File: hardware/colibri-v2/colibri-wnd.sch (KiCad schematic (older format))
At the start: 0 parts

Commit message: Work on GPS. Added PCA9685
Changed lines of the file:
@@
 $Descr A3 16535 11693
 encoding utf-8
-Sheet 1 25
+Sheet 1 26
 Title "Colibri WND"
 Date ""
@@
 	5350 4000 5750 4000
 Wire Wire Line
-	5750 4000 5750 6200
+	5750 4000 5750 5550
+Wire Wire Line
+	5750 5550 5750 6200
 Wire Wire Line
 	5750 6200 5350 6200
@@
 Text Notes 5500 2300 0    60   ~ 0
 Connect BUTTON_0 to:\nPB2/BOOT1
+$Sheet
+S 12850 8100 1850 750
+U 566CBCE8
+F0 "LED Controller" 60
+F1 "pca9685pw_led_ctrl.sch" 60
+F2 "PCA9685_OE(3V3)" I L 12850 8200 60
+F3 "PCA9865_I2C_SCL" I L 12850 8300 60
+F4 "PCA9865_I2C_SDA" B L 12850 8400 60
+$EndSheet
 $EndSCHEMATC

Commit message: Added connection between wandboard and cortex USB FS2
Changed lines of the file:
@@
 $Descr A3 16535 11693
 encoding utf-8
-Sheet 1 26
+Sheet 1 27
 Title "Colibri WND"
 Date ""
@@
 	5350 4000 5750 4000
 Wire Wire Line
-	5750 4000 5750 5550
-Wire Wire Line
-	5750 5550 5750 6200
+	5750 4000 5750 6200
 Wire Wire Line
 	5750 6200 5350 6200

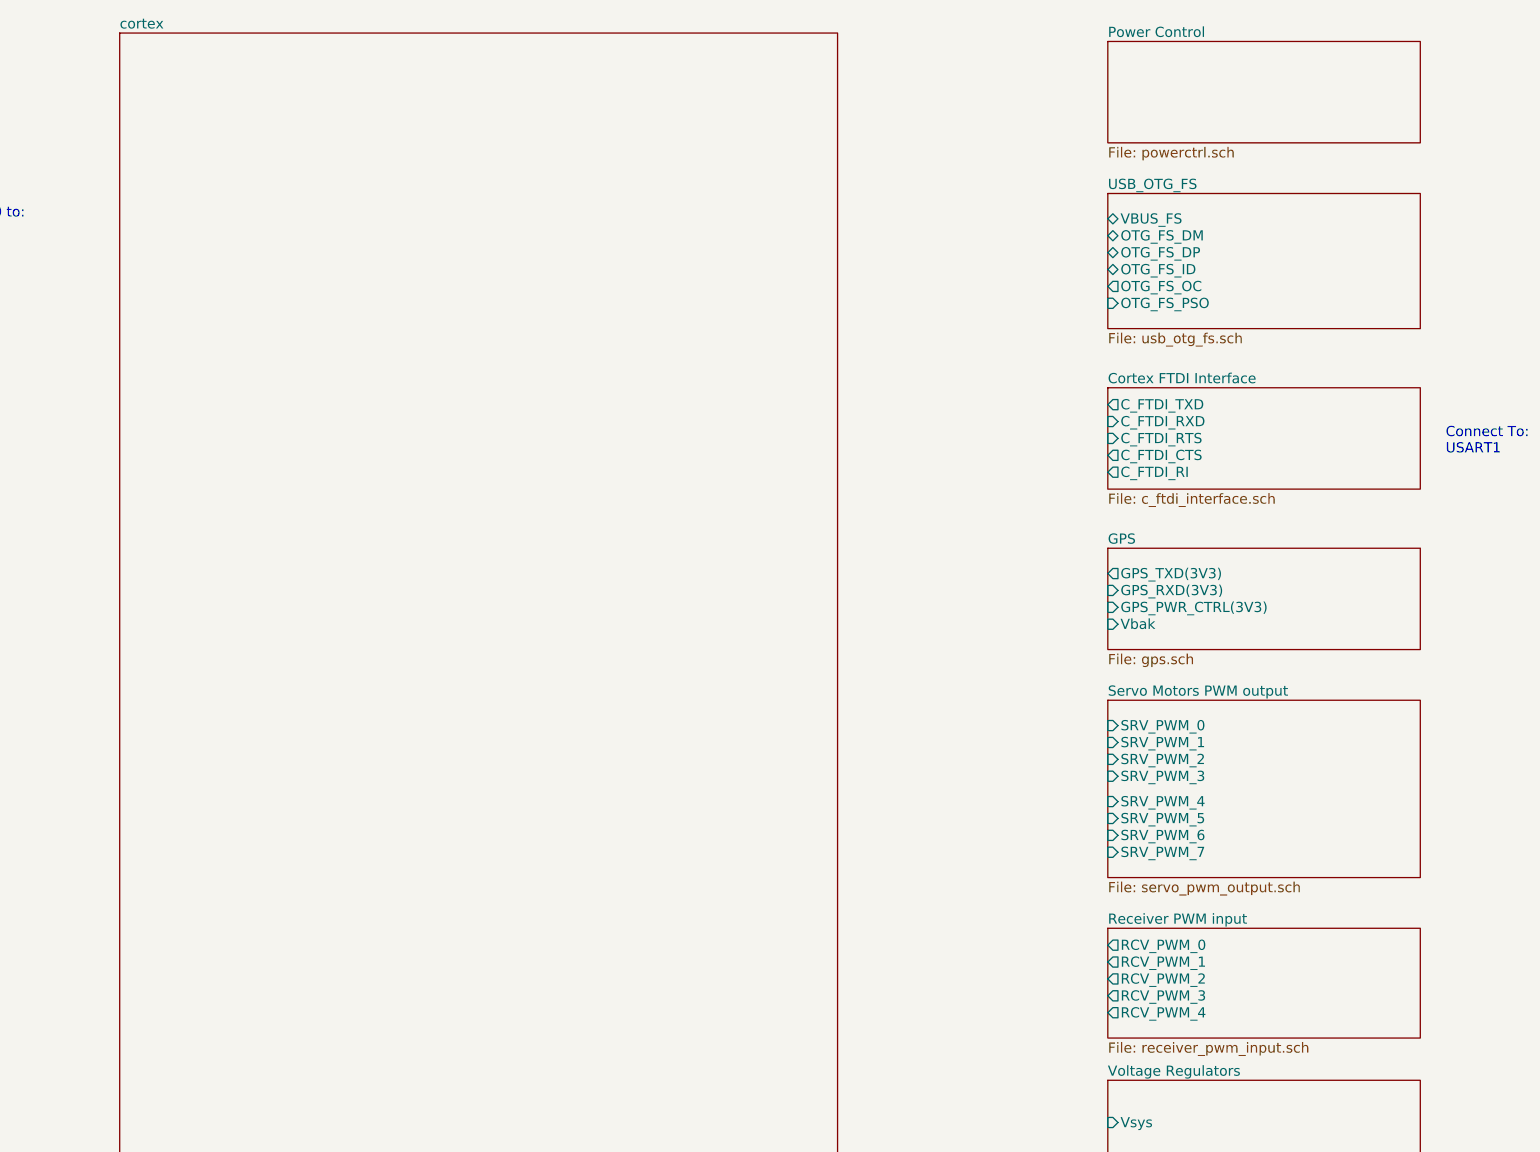
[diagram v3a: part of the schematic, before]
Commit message: Wired SDRAM pins. Added reset, power on/off for the WB module
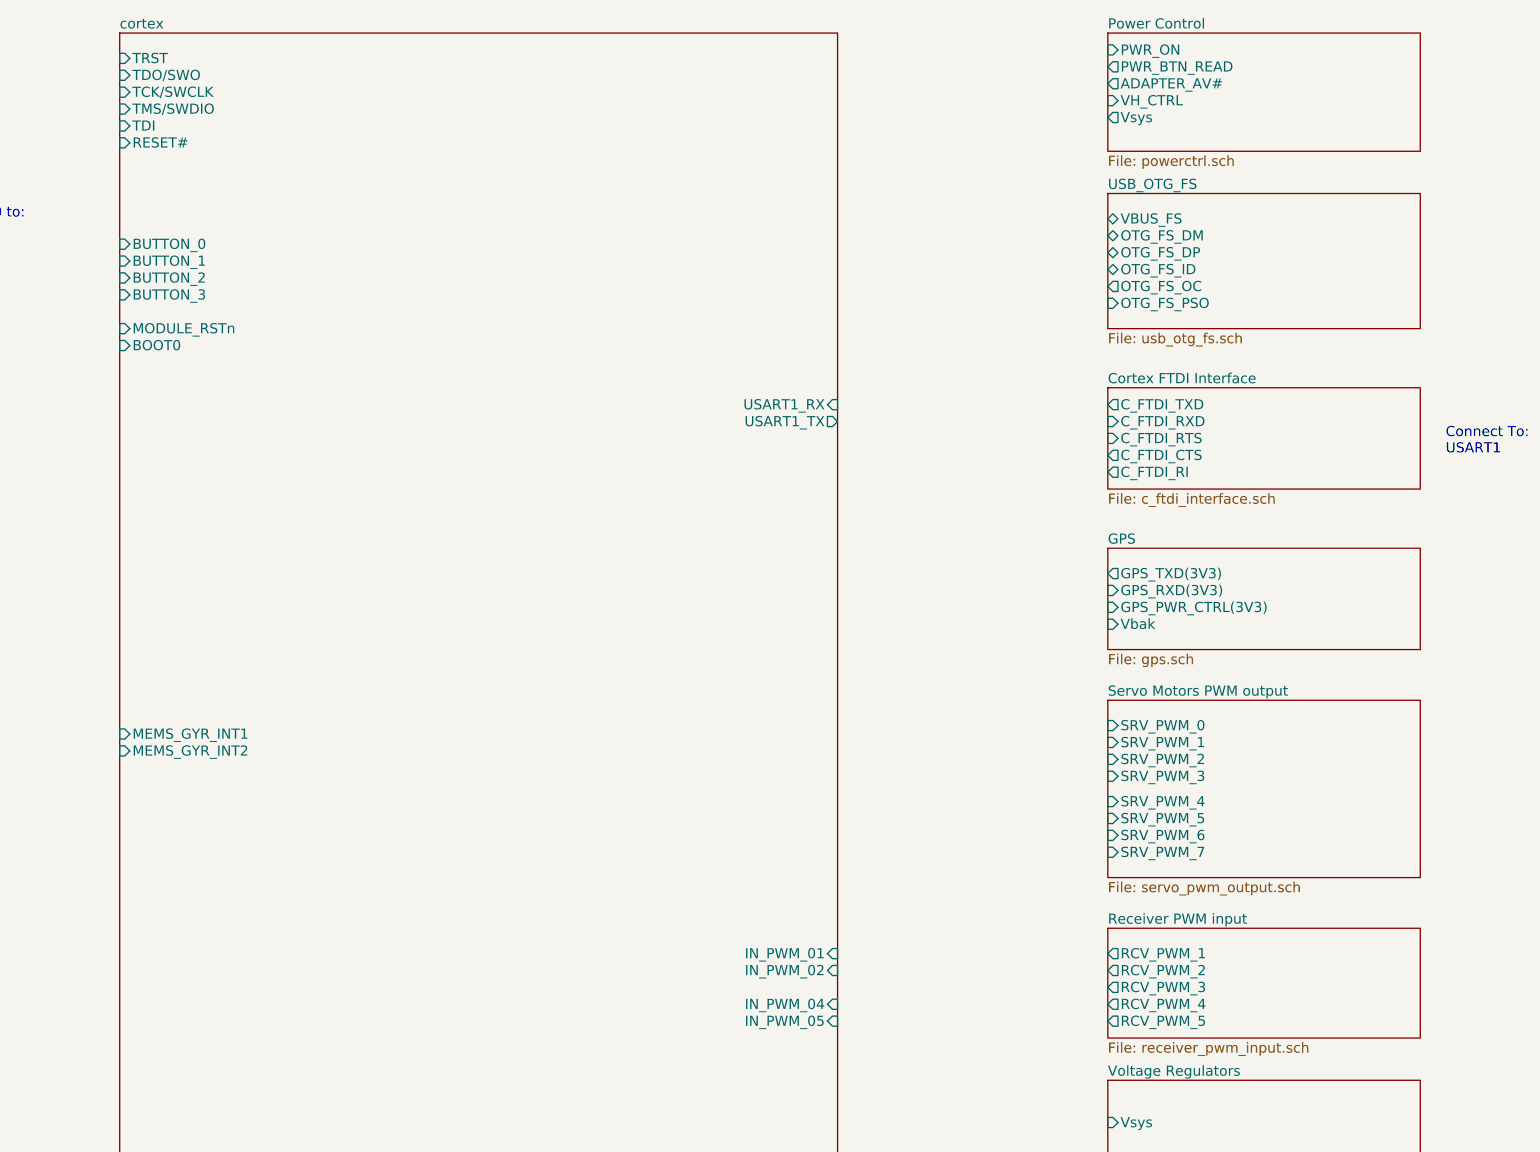
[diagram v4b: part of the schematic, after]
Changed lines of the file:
@@
 F0 "cortex" 60
 F1 "cortex.sch" 60
+F2 "TDI" I L 7000 1650 60
+F3 "TMS/SWDIO" I L 7000 1550 60
+F4 "TCK/SWCLK" I L 7000 1450 60
+F5 "RESET#" I L 7000 1750 60
+F6 "TRST" I L 7000 1250 60
+F7 "TDO/SWO" I L 7000 1350 60
+F8 "BOOT0" I L 7000 2950 60
+F9 "BUTTON_0" I L 7000 2350 60
+F10 "BUTTON_1" I L 7000 2450 60
+F11 "BUTTON_2" I L 7000 2550 60
+F12 "BUTTON_3" I L 7000 2650 60
+F13 "USART1_TX" O R 11250 3400 60
+F14 "USART1_RX" I R 11250 3300 60
+F15 "IN_PWM_04" I R 11250 6850 60
+F16 "MEMS_GYR_INT1" I L 7000 5250 60
+F17 "IN_PWM_05" I R 11250 6950 60
+F18 "MEMS_GYR_INT2" I L 7000 5350 60
+F19 "MODULE_RSTn" I L 7000 2850 60
+F20 "IN_PWM_01" I R 11250 6550 60
+F21 "IN_PWM_02" I R 11250 6650 60
 $EndSheet
 $Sheet
@@
 $EndSheet
 $Sheet
-S 12850 1150 1850 600
+S 12850 1100 1850 700
 U 5596276C
 F0 "Power Control" 60
 F1 "powerctrl.sch" 60
+F2 "VH_CTRL" I L 12850 1500 60
+F3 "Vsys" O L 12850 1600 60
+F4 "PWR_BTN_READ" O L 12850 1300 60
+F5 "ADAPTER_AV#" O L 12850 1400 60
+F6 "PWR_ON" I L 12850 1200 60
 $EndSheet
 $Sheet
@@
 F0 "Receiver PWM input" 60
 F1 "receiver_pwm_input.sch" 60
-F2 "RCV_PWM_0" O L 12850 6500 60
-F3 "RCV_PWM_1" O L 12850 6600 60
-F4 "RCV_PWM_2" O L 12850 6700 60
-F5 "RCV_PWM_3" O L 12850 6800 60
-F6 "RCV_PWM_4" O L 12850 6900 60
+F2 "RCV_PWM_1" O L 12850 6550 60
+F3 "RCV_PWM_2" O L 12850 6650 60
+F4 "RCV_PWM_3" O L 12850 6750 60
+F5 "RCV_PWM_4" O L 12850 6850 60
+F6 "RCV_PWM_5" O L 12850 6950 60
 $EndSheet
 $Sheet

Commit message: work on sheets wiring
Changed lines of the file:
@@
 $EndDescr
-$Sheet
-S 7000 1100 4250 8400
-U 557677C0
-F0 "cortex" 60
-F1 "cortex.sch" 60
-F2 "TDI" I L 7000 1650 60
-F3 "TMS/SWDIO" I L 7000 1550 60
-F4 "TCK/SWCLK" I L 7000 1450 60
-F5 "RESET#" I L 7000 1750 60
-F6 "TRST" I L 7000 1250 60
-F7 "TDO/SWO" I L 7000 1350 60
-F8 "BOOT0" I L 7000 2950 60
-F9 "BUTTON_0" I L 7000 2350 60
-F10 "BUTTON_1" I L 7000 2450 60
-F11 "BUTTON_2" I L 7000 2550 60
-F12 "BUTTON_3" I L 7000 2650 60
-F13 "USART1_TX" O R 11250 3400 60
-F14 "USART1_RX" I R 11250 3300 60
-F15 "IN_PWM_04" I R 11250 6850 60
-F16 "MEMS_GYR_INT1" I L 7000 5250 60
-F17 "IN_PWM_05" I R 11250 6950 60
-F18 "MEMS_GYR_INT2" I L 7000 5350 60
-F19 "MODULE_RSTn" I L 7000 2850 60
-F20 "IN_PWM_01" I R 11250 6550 60
-F21 "IN_PWM_02" I R 11250 6650 60
-$EndSheet
 $Sheet
 S 3500 1150 1850 800
@@
 $EndSheet
 $Sheet
-S 3500 2250 1850 1200
+S 3500 2200 1850 1250
 U 5586441E
 F0 "Leds/Buttons" 60
 F1 "leds_buttons.sch" 60
-F2 "BUTTON_0" O R 5350 2350 60
-F3 "BUTTON_1" O R 5350 2450 60
-F4 "BUTTON_2" O R 5350 2550 60
-F5 "BUTTON_3" O R 5350 2650 60
-F6 "BUTTON_4" O R 5350 2750 60
-F7 "RESET#" O R 5350 2850 60
-F8 "LED1" I R 5350 3050 60
-F9 "LED3" I R 5350 3250 60
-F10 "LED2" I R 5350 3150 60
-F11 "LED4" I R 5350 3350 60
-F12 "BOOT0" O R 5350 2950 60
+F2 "BUTTON_0" O R 5350 2400 60
+F3 "BUTTON_1" O R 5350 2500 60
+F4 "BUTTON_2" O R 5350 2600 60
+F5 "BUTTON_3" O R 5350 2700 60
+F6 "BUTTON_4" O R 5350 2800 60
+F7 "RESET#" O R 5350 2900 60
+F8 "LED1" I R 5350 3100 60
+F9 "LED3" I R 5350 3300 60
+F10 "LED2" I R 5350 3200 60
+F11 "LED4" I R 5350 3400 60
+F12 "BOOT0" O R 5350 2300 60
+F13 "MODULE_RESET#" O L 3500 3000 60
 $EndSheet
 $Sheet
@@
 $EndSheet
 $Sheet
-S 12850 1100 1850 700
+S 12850 950  1850 900
 U 5596276C
 F0 "Power Control" 60
 F1 "powerctrl.sch" 60
-F2 "VH_CTRL" I L 12850 1500 60
-F3 "Vsys" O L 12850 1600 60
-F4 "PWR_BTN_READ" O L 12850 1300 60
-F5 "ADAPTER_AV#" O L 12850 1400 60
-F6 "PWR_ON" I L 12850 1200 60
+F2 "VH_CTRL" I L 12850 1350 60
+F3 "Vsys" O L 12850 1450 60
+F4 "PWR_BTN_READ" O L 12850 1150 60
+F5 "ADAPTER_AV#" O L 12850 1250 60
+F6 "PWR_ON" I L 12850 1050 60
+F7 "JTAG_PWR_ON" I L 12850 1550 60
+F8 "BAT_MSRMNT" O L 12850 1650 60
+F9 "MSRMNT_ON" I L 12850 1750 60
 $EndSheet
 $Sheet
@@
 F0 "Wandboard Connector" 60
 F1 "wb_connector.sch" 60
+F2 "MODULE_RSTn" I L 3500 9300 60
+F3 "MODULE_ON/OFF" I R 5350 8100 60
 $EndSheet
 Wire Wire Line
@@
 Connection ~ 5750 5550
 $Sheet
-S 12850 4150 1850 600
+S 12850 4150 1850 650
 U 56138561
 F0 "GPS" 60
@@
 F4 "GPS_PWR_CTRL(3V3)" I L 12850 4500 60
 F5 "Vbak" I L 12850 4600 60
+F6 "GPS_TIME_PULSE" O L 12850 4700 60
 $EndSheet
 $Sheet
@@
 F4 "PCA9865_I2C_SDA" B L 12850 8400 60
 $EndSheet
+$Sheet
+S 7000 1100 4250 8400
+U 557677C0
+F0 "cortex" 60
+F1 "cortex.sch" 60
+F2 "TDI" I L 7000 1650 60
+F3 "TMS/SWDIO" I L 7000 1550 60
+F4 "TCK/SWCLK" I L 7000 1450 60
+F5 "RESET#" I L 7000 1750 60
+F6 "TRST" I L 7000 1250 60
+F7 "TDO/SWO" I L 7000 1350 60
+F8 "BOOT0" I L 7000 2300 60
+F9 "BUTTON_0" I L 7000 2400 60
+F10 "BUTTON_1" I L 7000 2500 60
+F11 "BUTTON_2" I L 7000 2600 60
+F12 "BUTTON_3" I L 7000 2700 60
+F13 "USART1_TX" O R 11250 3400 60
+F14 "USART1_RX" I R 11250 3300 60
+F15 "IN_PWM_04" I R 11250 6850 60
+F16 "MEMS_GYR_INT1" I L 7000 5250 60
+F17 "IN_PWM_05" I R 11250 6950 60
+F18 "MEMS_GYR_INT2" I L 7000 5350 60
+F19 "IN_PWM_01" I R 11250 6550 60
+F20 "IN_PWM_02" I R 11250 6650 60
+F21 "MODULE_RSTn" I L 7000 9300 60
+F22 "MODULE_ON/OFF" O L 7000 8100 60
+F23 "SRV_PWM_0" O R 11250 5200 60
+F24 "SRV_PWM_3" O R 11250 5500 60
+F25 "OTG_FS_VBUS" B R 11250 2200 60
+F26 "OTG_FS_ID" O R 11250 2500 60
+F27 "OTG_FS_DM" B R 11250 2300 60
+F28 "OTG_FS_DP" B R 11250 2400 60
+F29 "VH_CTRL" O R 11250 1350 60
+F30 "V_SENS_CTRL" O L 7000 3900 60
+F31 "GPS_TIME_PULSE" I R 11250 4700 60
+F32 "PS_I2C1_SCL" O L 7000 6100 60
+F33 "PS_I2C1_SDA" B L 7000 6000 60
+F34 "PCA9685_OE" O R 11250 8200 60
+F35 "OTG_HS_VBUS" B L 7000 8400 60
+F36 "OTG_HS_DM" B L 7000 8600 60
+F37 "OTG_HS_DP" B L 7000 8500 60
+F38 "PCA9685_SDA" B R 11250 8400 60
+F39 "PCA9685_SCL" O R 11250 8300 60
+F40 "MEMS_GYRO_CS" O L 7000 4750 60
+F41 "VBAT_MSRMNT" I R 11250 1650 60
+$EndSheet
+Text Label 2700 3000 0    60   ~ 0
+MODULE_RSTBTN
+Text Label 2700 9300 0    60   ~ 0
+MODULE_RSTBTN
+Wire Wire Line
+	2700 9300 3500 9300
+Wire Wire Line
+	2700 3000 3500 3000
+Text Label 6200 9300 0    60   ~ 0
+MODULE_RSTBTN
+Wire Wire Line
+	6200 9300 7000 9300
 $EndSCHEMATC

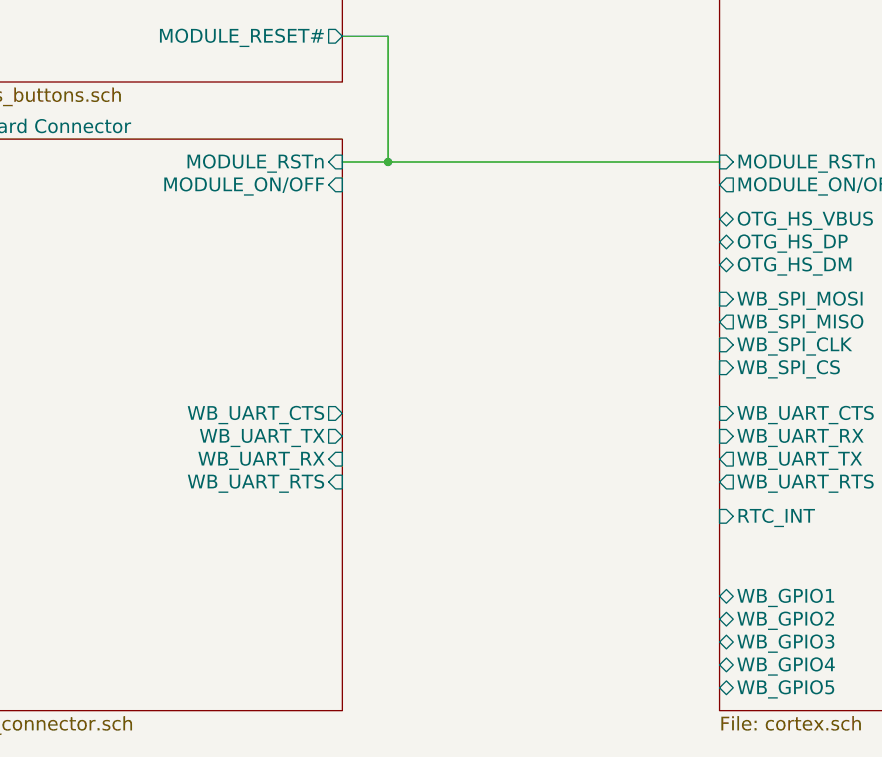
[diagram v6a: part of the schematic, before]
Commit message: Added M25P32
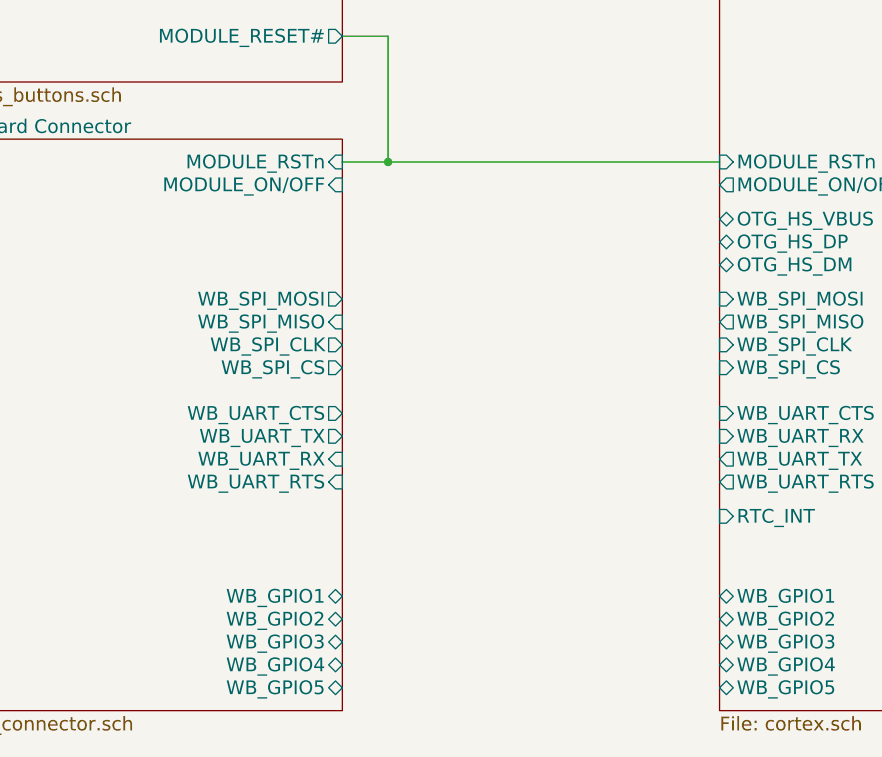
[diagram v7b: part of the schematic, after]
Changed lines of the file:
@@
 F6 "WB_UART_TX" O R 5350 8750 60
 F7 "WB_UART_RX" I R 5350 8850 60
+F8 "WB_SPI_MOSI" O R 5350 8150 60
+F9 "WB_SPI_MISO" I R 5350 8250 60
+F10 "WB_SPI_CLK" O R 5350 8350 60
+F11 "WB_SPI_CS" O R 5350 8450 60
+F12 "WB_GPIO1" B R 5350 9450 60
+F13 "WB_GPIO2" B R 5350 9550 60
+F14 "WB_GPIO3" B R 5350 9650 60
+F15 "WB_GPIO4" B R 5350 9750 60
+F16 "WB_GPIO5" B R 5350 9850 60
 $EndSheet
 $Sheet
@@
 $EndSheet
 Wire Wire Line
-	5350 7550 5550 7550
-Wire Wire Line
-	5550 7550 7000 7550
+	5350 7550 7000 7550
 Wire Wire Line
 	5350 7000 5550 7000
